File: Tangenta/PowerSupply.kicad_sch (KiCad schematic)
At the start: 5 parts, among them J1 39281243, U1 TPS54331DR, U2 TPS54331DR, U3 TPS54331DR, U4 TPS54331DR

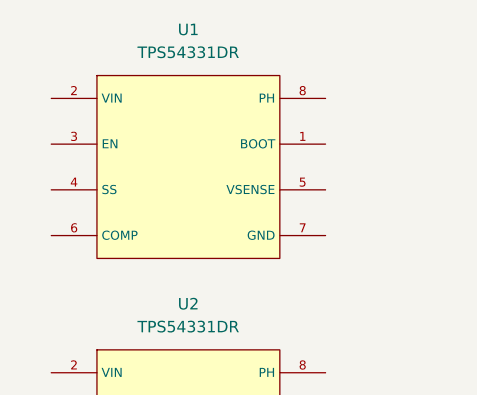
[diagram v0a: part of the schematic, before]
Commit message: Adding the TPS diode.
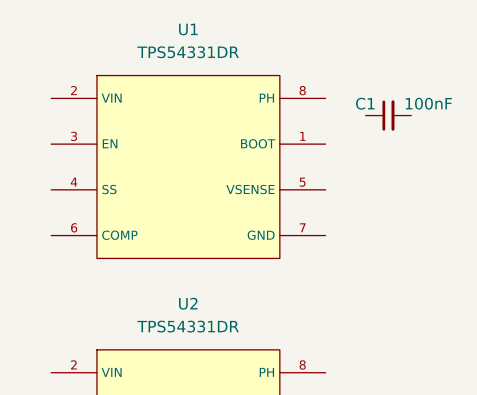
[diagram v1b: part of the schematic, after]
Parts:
- added C1: 100nF, symbol Device:C_Small
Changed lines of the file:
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@@
+    )
+  )
+  (symbol (lib_id "Device:C_Small") (at 212.725 37.465 90) (unit 1)
+    (in_bom yes) (on_board yes) (dnp no)
+    (property "Reference" "C1" (at 210.185 36.195 90)
+      (effects (font (size 1.27 1.27)))
+    )
+    (property "Value" "100nF" (at 217.17 36.195 90)
+      (effects (font (size 1.27 1.27)))
+    )
+    (property "Footprint" "" (at 212.725 37.465 0)
+      (effects (font (size 1.27 1.27)) hide)
+    )
+    (property "Datasheet" "~" (at 212.725 37.465 0)
+      (effects (font (size 1.27 1.27)) hide)
+    )
+    (pin "1")
+    (pin "2")
+    (instances
+      (project "Tangenta"
+        (path "/358d1bcf-7599-4352-8c4d-baa18a5f09e6/8215796b-9611-4f43-bcc5-319f8414b8a6"
+          (reference "C1") (unit 1)
+        )
+        (path "/358d1bcf-7599-4352-8c4d-baa18a5f09e6/d6c05402-162e-441f-bed8-be7996260fb4"
+          (reference "C2") (unit 1)
+        )
+      )
     )
   )

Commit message: Power supply - current progress.
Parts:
- added C1: 750pF, symbol Device:C_Small
- added C1: 8.2nF, symbol Device:C_Small
- added C1: 100pF, symbol Device:C_Small
- added C10: 47uF, CAP_TANTAL_A:CAP_TANTAL_A, symbol CAP_TANTAL_A:CA45-A-6_3V-47UF-K
- added C5: 47uF, CAP_L6:CAP_L6, symbol CAP_L6:35CE47AX
- added C6: 10uF, CAP_L6:CAP_L6, symbol CAP_L6:35CE47AX
- added D1: B540C-13-F, B540C-13-F:B540C-13-F, symbol B540C-13-F:B540C-13-F
- added L1: 6.8uH, Choke:Choke, symbol Choke:SLO0650H6R8MTT
- added R2: 39.2k, Resistor_SMD:R_0603_1608Metric, symbol Device:R_Small_US
- added R2: 41.2k, Resistor_SMD:R_0603_1608Metric, symbol Device:R_Small_US
- added R2: 10.2k, Resistor_SMD:R_0603_1608Metric, symbol Device:R_Small_US
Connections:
- net GND is gone; now on net GNDREF: J1.15, J1.17, J1.18, J1.19, J1.24, J1.3, J1.5, J1.7
- net 1V0: now also C10.1, C5.1, L1.1, R2.1
- net 5V: now also U1.2 (VIN), C6.1
- net at C1.1: now also U1.1 (BOOT)
- net at C1.2: now also U1.8 (PH), D1.1 (K), L1.2
- net GNDREF: now reaches U1.4 (SS)
- net GNDREF: now also U1.7 (GND), C1.1, C1.1, C1.1, C10.2, C5.2, C6.2, D1.2 (A), R2.2
- net at U1.5 (VSENSE): now also R2.1, R2.2
- net at U1.6 (COMP): now also C1.2, C1.2, R2.1
- new net: C1.2, R2.2
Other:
- moved on the sheet: C1

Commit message: Power supply - current progress.
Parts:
- added C1 (x3): 10pF, symbol Device:C_Small
- added C1: 2.7nF, symbol Device:C_Small
- added C1 (x3): 100nF, symbol Device:C_Small
- added C1 (x3): 8.2nF, symbol Device:C_Small
- added C1: 1.2nF, symbol Device:C_Small
- added C1: 1nF, symbol Device:C_Small
- added C11, C18, C25: 10uF, CAP_L6:CAP_L6, symbol CAP_L6:35CE47AX
- added C16, C23, C30: 47uF, CAP_L6:CAP_L6, symbol CAP_L6:35CE47AX
- added C17, C24, C31: 47uF, CAP_TANTAL_A:CAP_TANTAL_A, symbol CAP_TANTAL_A:CA45-A-6_3V-47UF-K
- added D2, D3, D4: B540C-13-F, B540C-13-F:B540C-13-F, symbol B540C-13-F:B540C-13-F
- added L2, L3, L4: 6.8uH, Choke:Choke, symbol Choke:SLO0650H6R8MTT
- added R2: 8.2k, Resistor_SMD:R_0603_1608Metric, symbol Device:R_Small_US
- added R2 (x3): 10.2k, Resistor_SMD:R_0603_1608Metric, symbol Device:R_Small_US
- added R2: 20.5k, Resistor_SMD:R_0603_1608Metric, symbol Device:R_Small_US
- added R2: 27.1k, Resistor_SMD:R_0603_1608Metric, symbol Device:R_Small_US
- added R2: 11.3k, Resistor_SMD:R_0603_1608Metric, symbol Device:R_Small_US
- added R2: 25.5k, Resistor_SMD:R_0603_1608Metric, symbol Device:R_Small_US
- added R2: 4.81k, Resistor_SMD:R_0603_1608Metric, symbol Device:R_Small_US
- C1: value 8.2nF -> 100pF
- C1: value 100pF -> 8.2nF
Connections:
- net 1V1: now also C16.1, C17.1, L2.1, R2.1
- net 1V8: now also C23.1, C24.1, L3.1, R2.1
- net 2V5: now also C30.1, C31.1, L4.1, R2.1
- net 5V: now also U2.2 (VIN), U3.2 (VIN), U4.2 (VIN), C11.1, C18.1, C25.1
- net GNDREF: now also U2.7 (GND), U3.7 (GND), U4.7 (GND), C1.1, C1.1, C1.1, C1.1, C1.1, C1.1, C1.1, C1.1, C1.1, C11.2, C16.2, C17.2, C18.2, C23.2, C24.2, C25.2, C30.2, C31.2, D2.2 (A), D3.2 (A), D4.2 (A), R2.2, R2.2, R2.2; no longer U1.4 (SS)
- net at U2.1 (BOOT): now also C1.1
- net at U2.4 (SS): now also C1.2
- net at U2.5 (VSENSE): now also R2.1, R2.2
- net at U2.6 (COMP): now also C1.2, R2.1
- net at U2.8 (PH): now also C1.2, D2.1 (K), L2.2
- net at C1.2, R2.1, U1.6 (COMP): no longer C1.2
- net at U3.1 (BOOT): now also C1.1
- net at U3.4 (SS): now also C1.2
- net at U3.5 (VSENSE): now also R2.1, R2.2
- net at U3.6 (COMP): now also C1.2, R2.1
- net at U3.8 (PH): now also C1.2, D3.1 (K), L3.2
- net at U4.1 (BOOT): now also C1.1
- net at U4.4 (SS): now also C1.2
- net at U4.5 (VSENSE): now also R2.1, R2.2
- net at U4.6 (COMP): now also C1.2, R2.1
- net at U4.8 (PH): now also C1.2, D4.1 (K), L4.2
- new net: C1.2, R2.2 (x3)
- new net: C1.2, U1.4 (SS)
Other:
- moved on the sheet: C1, C10, C5, C6, D1, J1, L1, R2, U1, U2, U3, U4

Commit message: Current progress...
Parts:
- C1: footprint (none) -> Capacitor_SMD:C_0603_1608Metric
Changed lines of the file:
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@@
       (effects (font (size 1.27 1.27)))
     )
-    (property "Footprint" "" (at 62.865 49.53 0)
+    (property "Footprint" "Capacitor_SMD:C_0603_1608Metric" (at 62.865 49.53 0)
       (effects (font (size 1.27 1.27)) hide)
     )
@@
       (effects (font (size 1.27 1.27)))
     )
-    (property "Footprint" "" (at 51.435 88.9 0)
+    (property "Footprint" "Capacitor_SMD:C_0603_1608Metric" (at 51.435 88.9 0)
       (effects (font (size 1.27 1.27)) hide)
     )
@@
       (effects (font (size 1.27 1.27)))
     )
-    (property "Footprint" "" (at 51.435 49.53 0)
+    (property "Footprint" "Capacitor_SMD:C_0603_1608Metric" (at 51.435 49.53 0)
       (effects (font (size 1.27 1.27)) hide)
     )
@@
       (effects (font (size 1.27 1.27)))
     )
-    (property "Footprint" "" (at 62.865 88.9 0)
+    (property "Footprint" "Capacitor_SMD:C_0603_1608Metric" (at 62.865 88.9 0)
       (effects (font (size 1.27 1.27)) hide)
     )
@@
       (effects (font (size 1.27 1.27)))
     )
-    (property "Footprint" "" (at 107.315 146.685 0)
+    (property "Footprint" "Capacitor_SMD:C_0603_1608Metric" (at 107.315 146.685 0)
       (effects (font (size 1.27 1.27)) hide)
     )
@@
       (effects (font (size 1.27 1.27)))
     )
-    (property "Footprint" "" (at 107.315 66.04 0)
+    (property "Footprint" "Capacitor_SMD:C_0603_1608Metric" (at 107.315 66.04 0)
       (effects (font (size 1.27 1.27)) hide)
     )
@@
       (effects (font (size 1.27 1.27)))
     )
-    (property "Footprint" "" (at 40.005 128.905 0)
+    (property "Footprint" "Capacitor_SMD:C_0603_1608Metric" (at 40.005 128.905 0)
       (effects (font (size 1.27 1.27)) hide)
     )
@@
       (effects (font (size 1.27 1.27)))
     )
-    (property "Footprint" "" (at 62.865 128.905 0)
+    (property "Footprint" "Capacitor_SMD:C_0603_1608Metric" (at 62.865 128.905 0)
       (effects (font (size 1.27 1.27)) hide)
     )
@@
       (effects (font (size 1.27 1.27)))
     )
-    (property "Footprint" "" (at 40.005 49.53 0)
+    (property "Footprint" "Capacitor_SMD:C_0603_1608Metric" (at 40.005 49.53 0)
       (effects (font (size 1.27 1.27)) hide)
     )
@@
       (effects (font (size 1.27 1.27)))
     )
-    (property "Footprint" "" (at 107.315 106.045 0)
+    (property "Footprint" "Capacitor_SMD:C_0603_1608Metric" (at 107.315 106.045 0)
       (effects (font (size 1.27 1.27)) hide)
     )
@@
       (effects (font (size 1.27 1.27)))
     )
-    (property "Footprint" "" (at 51.435 128.905 0)
+    (property "Footprint" "Capacitor_SMD:C_0603_1608Metric" (at 51.435 128.905 0)
       (effects (font (size 1.27 1.27)) hide)
     )
@@
       (effects (font (size 1.27 1.27)))
     )
-    (property "Footprint" "" (at 40.005 169.545 0)
+    (property "Footprint" "Capacitor_SMD:C_0603_1608Metric" (at 40.005 169.545 0)
       (effects (font (size 1.27 1.27)) hide)
     )
@@
       (effects (font (size 1.27 1.27)))
     )
-    (property "Footprint" "" (at 107.315 26.67 0)
+    (property "Footprint" "Capacitor_SMD:C_0603_1608Metric" (at 107.315 26.67 0)
       (effects (font (size 1.27 1.27)) hide)
     )
@@
       (effects (font (size 1.27 1.27)))
     )
-    (property "Footprint" "" (at 40.005 88.9 0)
+    (property "Footprint" "Capacitor_SMD:C_0603_1608Metric" (at 40.005 88.9 0)
       (effects (font (size 1.27 1.27)) hide)
     )
@@
       (effects (font (size 1.27 1.27)))
     )
-    (property "Footprint" "" (at 62.865 169.545 0)
+    (property "Footprint" "Capacitor_SMD:C_0603_1608Metric" (at 62.865 169.545 0)
       (effects (font (size 1.27 1.27)) hide)
     )
@@
       (effects (font (size 1.27 1.27)))
     )
-    (property "Footprint" "" (at 51.435 169.545 0)
-      (effects (font (size 1.27 1.27)) hide)
-    )
+    (property "Footprint" "Capacitor_SMD:C_0603_1608Metric" (at 51.435 169.545 0)
+      (effects (font (size 1.27 1.27)) hide)
+    )

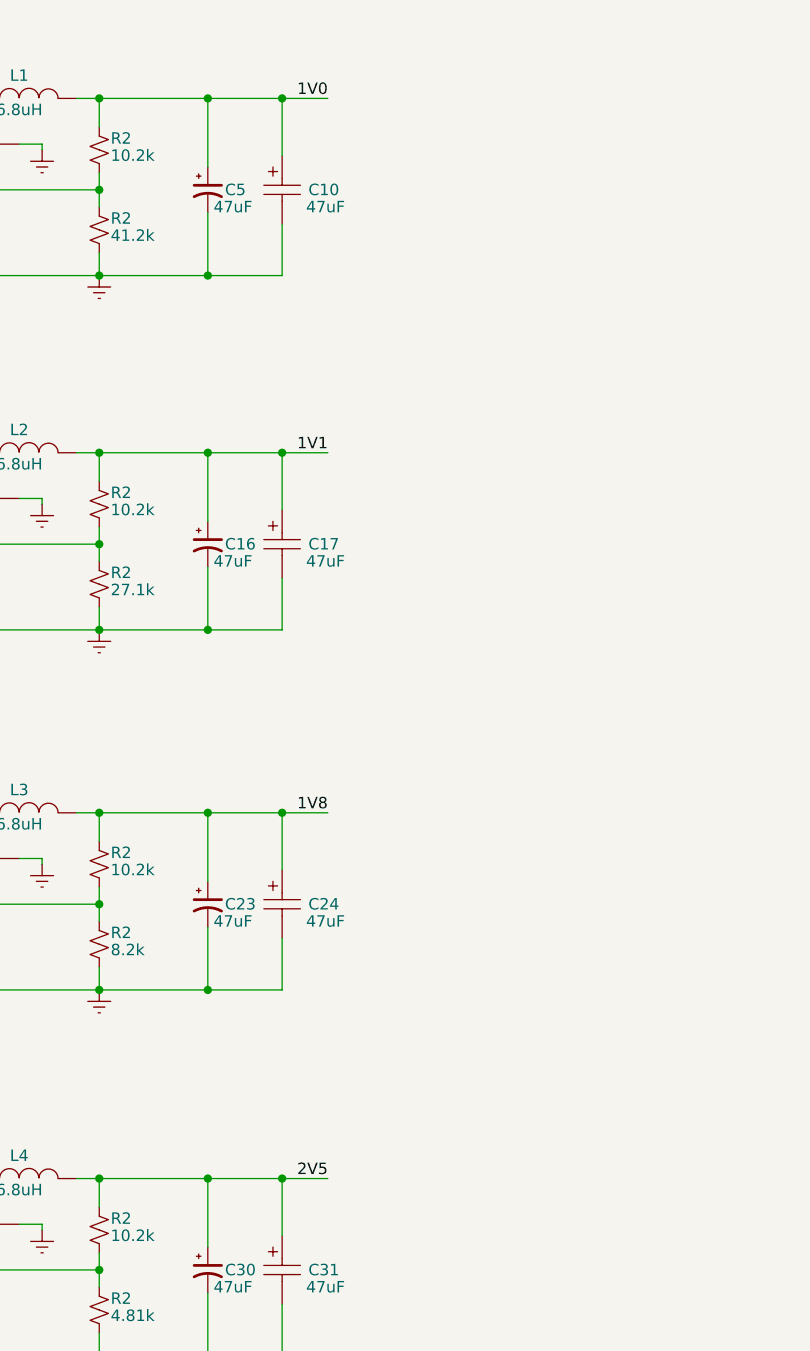
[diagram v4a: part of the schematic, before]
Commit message: Power supply jumpers.
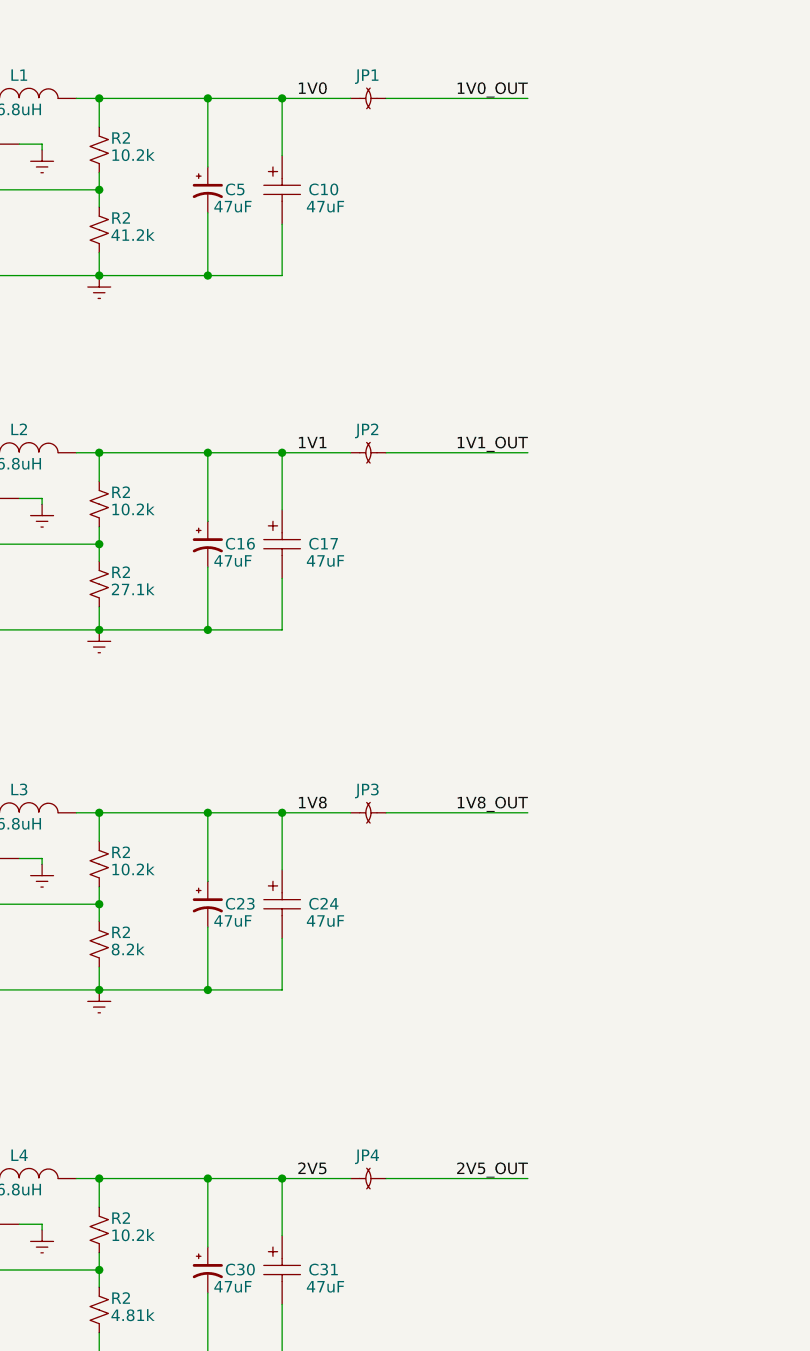
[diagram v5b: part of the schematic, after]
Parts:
- added JP1, JP2, JP3, JP4: ~, CustomJumper:R_0805_2012Metric, symbol CustomJumper:CustomJumper
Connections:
- net 1V0: now also JP1.1
- net 1V1: now also JP2.1
- net 1V8: now also JP3.1
- net 2V5: now also JP4.1
- new net 1V0_OUT: JP1.2
- new net 1V1_OUT: JP2.2
- new net 1V8_OUT: JP3.2
- new net 2V5_OUT: JP4.2
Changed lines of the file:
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@@
+    (stroke (width 0) (type default))
+  )
+  (wire (pts (xy 163.322 24.13) (xy 179.07 24.13))
     (stroke (width 0) (type default))
   )
@@
     (stroke (width 0) (type default))
   )
-  (wire (pts (xy 151.765 63.5) (xy 156.845 63.5))
+  (wire (pts (xy 151.765 63.5) (xy 159.385 63.5))
     (stroke (width 0) (type default))
   )
@@
     (stroke (width 0) (type default))
   )
+  (wire (pts (xy 163.322 103.505) (xy 179.07 103.505))
+    (stroke (width 0) (type default))
+  )
   (wire (pts (xy 51.435 137.795) (xy 51.435 131.445))
     (stroke (width 0) (type default))
@@
     (stroke (width 0) (type default))
   )
+  (wire (pts (xy 163.322 144.145) (xy 179.07 144.145))
+    (stroke (width 0) (type default))
+  )
   (wire (pts (xy 131.445 83.185) (xy 143.51 83.185))
     (stroke (width 0) (type default))
@@
     (stroke (width 0) (type default))
   )
-  (wire (pts (xy 151.765 144.145) (xy 156.845 144.145))
+  (wire (pts (xy 151.765 144.145) (xy 159.385 144.145))
     (stroke (width 0) (type default))
   )
@@
     (stroke (width 0) (type default))
   )
-  (wire (pts (xy 151.765 103.505) (xy 156.845 103.505))
+  (wire (pts (xy 151.765 103.505) (xy 159.385 103.505))
     (stroke (width 0) (type default))
   )
@@
     (stroke (width 0) (type default))
   )
+  (wire (pts (xy 163.322 63.5) (xy 179.07 63.5))
+    (stroke (width 0) (type default))
+  )
   (wire (pts (xy 30.48 178.435) (xy 40.005 178.435))
     (stroke (width 0) (type default))
@@
     (stroke (width 0) (type default))
   )
-  (wire (pts (xy 151.765 24.13) (xy 156.845 24.13))
+  (wire (pts (xy 151.765 24.13) (xy 159.385 24.13))
     (stroke (width 0) (type default))
   )
@@
     (effects (font (size 1.27 1.27)) (justify right bottom))
   )
+  (label "2V5_OUT" (at 179.07 144.145 180) (fields_autoplaced)
+    (effects (font (size 1.27 1.27)) (justify right bottom))
+  )
   (label "GND" (at 237.871 41.91 0) (fields_autoplaced)
     (effects (font (size 1.27 1.27)) (justify left bottom))
@@
     (effects (font (size 1.27 1.27)) (justify right bottom))
   )
+  (label "1V8_OUT" (at 179.07 103.505 180) (fields_autoplaced)
+    (effects (font (size 1.27 1.27)) (justify right bottom))
+  )
   (label "1V8" (at 156.845 103.505 180) (fields_autoplaced)
     (effects (font (size 1.27 1.27)) (justify right bottom))
@@
     (effects (font (size 1.27 1.27)) (justify left bottom))
   )
+  (label "1V0_OUT" (at 179.07 24.13 180) (fields_autoplaced)
+    (effects (font (size 1.27 1.27)) (justify right bottom))
+  )
   (label "3V3" (at 217.551 26.67 180) (fields_autoplaced)
     (effects (font (size 1.27 1.27)) (justify right bottom))
@@
   )
   (label "12V" (at 217.551 49.53 180) (fields_autoplaced)
+    (effects (font (size 1.27 1.27)) (justify right bottom))
+  )
+  (label "1V1_OUT" (at 179.07 63.5 180) (fields_autoplaced)
     (effects (font (size 1.27 1.27)) (justify right bottom))
   )
@@
     )
   )
+  (symbol (lib_id "CustomJumper:CustomJumper") (at 161.29 141.859 0) (unit 1)
+    (in_bom yes) (on_board yes) (dnp no)
+    (property "Reference" "JP4" (at 161.29 141.605 0)
+      (effects (font (size 1.27 1.27)))
+    )
+    (property "Value" "~" (at 161.29 141.859 0)
+      (effects (font (size 1.27 1.27)))
+    )
+    (property "Footprint" "CustomJumper:R_0805_2012Metric" (at 163.576 146.685 0)
+      (effects (font (size 1.27 1.27)) hide)
+    )
+    (property "Datasheet" "" (at 161.29 141.859 0)
+      (effects (font (size 1.27 1.27)) hide)
+    )
+    (pin "1")
+    (pin "2")
+    (instances
+      (project "Tangenta"
+        (path "/358d1bcf-7599-4352-8c4d-baa18a5f09e6/d6c05402-162e-441f-bed8-be7996260fb4"
+          (reference "JP4") (unit 1)
+        )
+      )
+    )
+  )
   (symbol (lib_id "Device:R_Small_US") (at 62.865 122.555 0) (mirror y) (unit 1)
     (in_bom yes) (on_board yes) (dnp no)
@@
         (path "/358d1bcf-7599-4352-8c4d-baa18a5f09e6/d6c05402-162e-441f-bed8-be7996260fb4"
           (reference "R16") (unit 1)
+        )
+      )
+    )
+  )
+  (symbol (lib_id "CustomJumper:CustomJumper") (at 161.29 101.219 0) (unit 1)
+    (in_bom yes) (on_board yes) (dnp no)
+    (property "Reference" "JP3" (at 161.29 100.965 0)
+      (effects (font (size 1.27 1.27)))
+    )
+    (property "Value" "~" (at 161.29 101.219 0)
+      (effects (font (size 1.27 1.27)))
+    )
+    (property "Footprint" "CustomJumper:R_0805_2012Metric" (at 163.576 106.045 0)
+      (effects (font (size 1.27 1.27)) hide)
+    )
+    (property "Datasheet" "" (at 161.29 101.219 0)
+      (effects (font (size 1.27 1.27)) hide)
+    )
+    (pin "1")
+    (pin "2")
+    (instances
+      (project "Tangenta"
+        (path "/358d1bcf-7599-4352-8c4d-baa18a5f09e6/d6c05402-162e-441f-bed8-be7996260fb4"
+          (reference "JP3") (unit 1)
         )
       )
@@
     )
   )
+  (symbol (lib_id "CustomJumper:CustomJumper") (at 161.29 21.844 0) (unit 1)
+    (in_bom yes) (on_board yes) (dnp no)
+    (property "Reference" "JP1" (at 161.29 21.59 0)
+      (effects (font (size 1.27 1.27)))
+    )
+    (property "Value" "~" (at 161.29 21.844 0)
+      (effects (font (size 1.27 1.27)))
+    )
+    (property "Footprint" "CustomJumper:R_0805_2012Metric" (at 163.576 26.67 0)
+      (effects (font (size 1.27 1.27)) hide)
+    )
+    (property "Datasheet" "" (at 161.29 21.844 0)
+      (effects (font (size 1.27 1.27)) hide)
+    )
+    (pin "1")
+    (pin "2")
+    (instances
+      (project "Tangenta"
+        (path "/358d1bcf-7599-4352-8c4d-baa18a5f09e6/d6c05402-162e-441f-bed8-be7996260fb4"
+          (reference "JP1") (unit 1)
+        )
+      )
+    )
+  )
   (symbol (lib_id "B540C-13-F:B540C-13-F") (at 117.475 149.225 0) (unit 1)
     (in_bom yes) (on_board yes) (dnp no)
@@
         )
       )
+    )
+  )
+  (symbol (lib_id "CustomJumper:CustomJumper") (at 161.29 61.214 0) (unit 1)
+    (in_bom yes) (on_board yes) (dnp no)
+    (property "Reference" "JP2" (at 161.29 60.96 0)
+      (effects (font (size 1.27 1.27)))
+    )
+    (property "Value" "~" (at 161.29 61.214 0)
+      (effects (font (size 1.27 1.27)))
+    )
+    (property "Footprint" "CustomJumper:R_0805_2012Metric" (at 163.576 66.04 0)
+      (effects (font (size 1.27 1.27)) hide)
+    )
+    (property "Datasheet" "" (at 161.29 61.214 0)
+      (effects (font (size 1.27 1.27)) hide)
+    )
+    (pin "1")
+    (pin "2")
+    (instances
+      (project "Tangenta"
+        (path "/358d1bcf-7599-4352-8c4d-baa18a5f09e6/d6c05402-162e-441f-bed8-be7996260fb4"
+          (reference "JP2") (unit 1)
+        )
+      )

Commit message: Current progress with the USB schematics...
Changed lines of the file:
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@@
     (stroke (width 0) (type default))
   )
-  (text "24-pin ATX Connector" (at 217.297 19.177 0)
+  (text "24-pin ATX Connector" (at 216.535 20.955 0)
     (effects (font (size 1.27 1.27)) (justify left bottom))
   )
